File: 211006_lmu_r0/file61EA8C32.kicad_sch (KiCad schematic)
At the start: 15 parts, among them U7 ADuM7641A

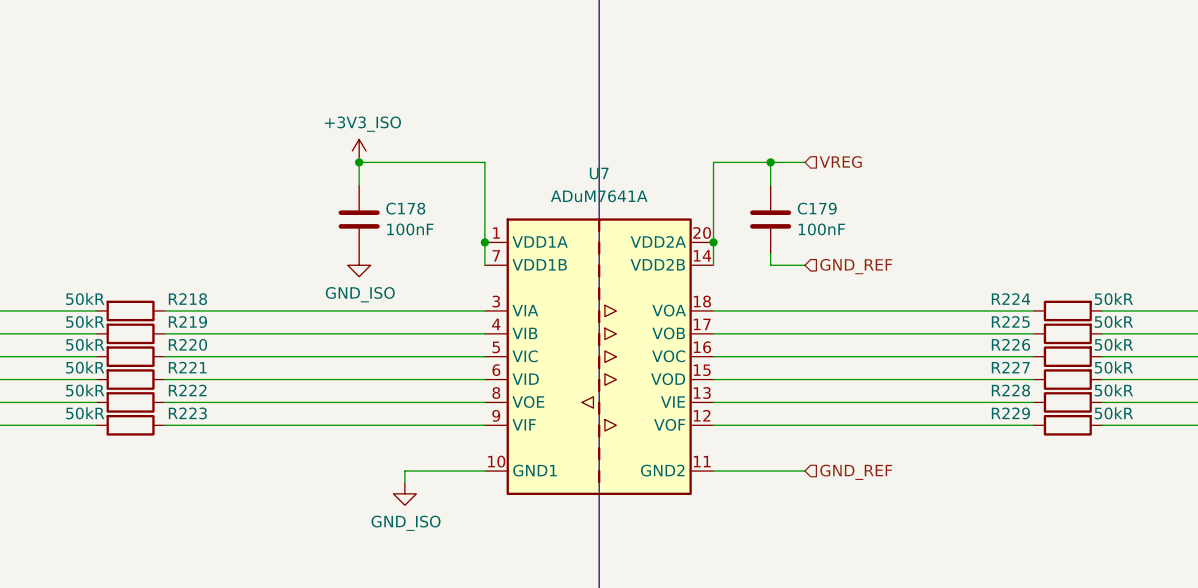
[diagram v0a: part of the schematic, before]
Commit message: moved micro into position
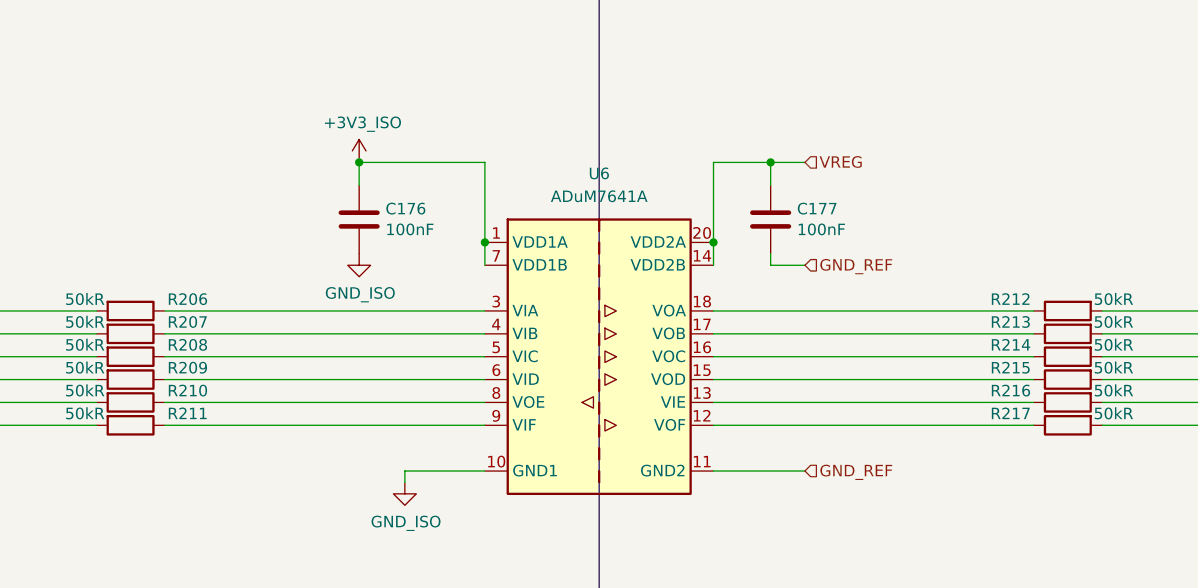
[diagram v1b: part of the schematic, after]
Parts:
- renumbered C178 to C176, C179 to C177, R218 to R206, R219 to R207, R220 to R208, R221 to R209, R222 to R210, R223 to R211, R224 to R212, R225 to R213, R226 to R214, R227 to R215, R228 to R216, R229 to R217, U7 to U6
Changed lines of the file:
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@@
   (symbol (lib_id "Device:C") (at 118.11 83.82 0)
     (in_bom yes) (on_board yes)
-    (property "Reference" "C178" (id 0) (at 121.031 82.6516 0)
+    (property "Reference" "C176" (id 0) (at 121.031 82.6516 0)
       (effects (font (size 1.27 1.27)) (justify left))
     )
@@
   (symbol (lib_id "Device:R") (at 92.71 101.6 270)
     (in_bom yes) (on_board yes)
-    (property "Reference" "R221" (id 0) (at 99.06 100.33 90))
+    (property "Reference" "R209" (id 0) (at 99.06 100.33 90))
     (property "Value" "50kR" (id 1) (at 87.63 100.33 90))
     (property "Footprint" "Resistor_SMD:R_0603_1608Metric_Pad0.98x0.95mm_HandSolder" (id 2) (at 92.71 99.822 90)
@@
   (symbol (lib_id "Device:R") (at 92.71 93.98 270)
     (in_bom yes) (on_board yes)
-    (property "Reference" "R218" (id 0) (at 99.06 92.71 90))
+    (property "Reference" "R206" (id 0) (at 99.06 92.71 90))
     (property "Value" "50kR" (id 1) (at 87.63 92.71 90))
     (property "Footprint" "Resistor_SMD:R_0603_1608Metric_Pad0.98x0.95mm_HandSolder" (id 2) (at 92.71 92.202 90)
@@
   (symbol (lib_id "Device:R") (at 196.85 99.06 90) (mirror x)
     (in_bom yes) (on_board yes)
-    (property "Reference" "R226" (id 0) (at 190.5 97.79 90))
+    (property "Reference" "R214" (id 0) (at 190.5 97.79 90))
     (property "Value" "50kR" (id 1) (at 201.93 97.79 90))
     (property "Footprint" "Resistor_SMD:R_0603_1608Metric_Pad0.98x0.95mm_HandSolder" (id 2) (at 196.85 97.282 90)
@@
   (symbol (lib_id "Device:R") (at 92.71 99.06 270)
     (in_bom yes) (on_board yes)
-    (property "Reference" "R220" (id 0) (at 99.06 97.79 90))
+    (property "Reference" "R208" (id 0) (at 99.06 97.79 90))
     (property "Value" "50kR" (id 1) (at 87.63 97.79 90))
     (property "Footprint" "Resistor_SMD:R_0603_1608Metric_Pad0.98x0.95mm_HandSolder" (id 2) (at 92.71 97.282 90)
@@
   (symbol (lib_id "Device:R") (at 92.71 106.68 270)
     (in_bom yes) (on_board yes)
-    (property "Reference" "R223" (id 0) (at 99.06 105.41 90))
+    (property "Reference" "R211" (id 0) (at 99.06 105.41 90))
     (property "Value" "50kR" (id 1) (at 87.63 105.41 90))
     (property "Footprint" "Resistor_SMD:R_0603_1608Metric_Pad0.98x0.95mm_HandSolder" (id 2) (at 92.71 104.902 90)
@@
   (symbol (lib_id "Device:R") (at 92.71 96.52 270)
     (in_bom yes) (on_board yes)
-    (property "Reference" "R219" (id 0) (at 99.06 95.25 90))
+    (property "Reference" "R207" (id 0) (at 99.06 95.25 90))
     (property "Value" "50kR" (id 1) (at 87.63 95.25 90))
     (property "Footprint" "Resistor_SMD:R_0603_1608Metric_Pad0.98x0.95mm_HandSolder" (id 2) (at 92.71 94.742 90)
@@
   (symbol (lib_id "Device:R") (at 196.85 93.98 90) (mirror x)
     (in_bom yes) (on_board yes)
-    (property "Reference" "R224" (id 0) (at 190.5 92.71 90))
+    (property "Reference" "R212" (id 0) (at 190.5 92.71 90))
     (property "Value" "50kR" (id 1) (at 201.93 92.71 90))
     (property "Footprint" "Resistor_SMD:R_0603_1608Metric_Pad0.98x0.95mm_HandSolder" (id 2) (at 196.85 92.202 90)
@@
   (symbol (lib_id "Isolator:ADuM7641A") (at 144.78 99.06 0)
     (in_bom yes) (on_board yes) (fields_autoplaced)
-    (property "Reference" "U7" (id 0) (at 144.78 78.74 0))
+    (property "Reference" "U6" (id 0) (at 144.78 78.74 0))
     (property "Value" "ADuM7641A" (id 1) (at 144.78 81.28 0))
     (property "Footprint" "Package_SO:QSOP-20_3.9x8.7mm_P0.635mm" (id 2) (at 144.78 116.84 0)
@@
   (symbol (lib_id "Device:R") (at 196.85 101.6 90) (mirror x)
     (in_bom yes) (on_board yes)
-    (property "Reference" "R227" (id 0) (at 190.5 100.33 90))
+    (property "Reference" "R215" (id 0) (at 190.5 100.33 90))
     (property "Value" "50kR" (id 1) (at 201.93 100.33 90))
     (property "Footprint" "Resistor_SMD:R_0603_1608Metric_Pad0.98x0.95mm_HandSolder" (id 2) (at 196.85 99.822 90)
@@
   (symbol (lib_id "Device:R") (at 92.71 104.14 270)
     (in_bom yes) (on_board yes)
-    (property "Reference" "R222" (id 0) (at 99.06 102.87 90))
+    (property "Reference" "R210" (id 0) (at 99.06 102.87 90))
     (property "Value" "50kR" (id 1) (at 87.63 102.87 90))
     (property "Footprint" "Resistor_SMD:R_0603_1608Metric_Pad0.98x0.95mm_HandSolder" (id 2) (at 92.71 102.362 90)
@@
   (symbol (lib_id "Device:R") (at 196.85 96.52 90) (mirror x)
     (in_bom yes) (on_board yes)
-    (property "Reference" "R225" (id 0) (at 190.5 95.25 90))
+    (property "Reference" "R213" (id 0) (at 190.5 95.25 90))
     (property "Value" "50kR" (id 1) (at 201.93 95.25 90))
     (property "Footprint" "Resistor_SMD:R_0603_1608Metric_Pad0.98x0.95mm_HandSolder" (id 2) (at 196.85 94.742 90)
@@
   (symbol (lib_id "Device:R") (at 196.85 104.14 90) (mirror x)
     (in_bom yes) (on_board yes)
-    (property "Reference" "R228" (id 0) (at 190.5 102.87 90))
+    (property "Reference" "R216" (id 0) (at 190.5 102.87 90))
     (property "Value" "50kR" (id 1) (at 201.93 102.87 90))
     (property "Footprint" "Resistor_SMD:R_0603_1608Metric_Pad0.98x0.95mm_HandSolder" (id 2) (at 196.85 102.362 90)
@@
   (symbol (lib_id "Device:C") (at 163.83 83.82 0)
     (in_bom yes) (on_board yes)
-    (property "Reference" "C179" (id 0) (at 166.751 82.6516 0)
+    (property "Reference" "C177" (id 0) (at 166.751 82.6516 0)
       (effects (font (size 1.27 1.27)) (justify left))
     )
@@
   (symbol (lib_id "Device:R") (at 196.85 106.68 90) (mirror x)
     (in_bom yes) (on_board yes)
-    (property "Reference" "R229" (id 0) (at 190.5 105.41 90))
+    (property "Reference" "R217" (id 0) (at 190.5 105.41 90))
     (property "Value" "50kR" (id 1) (at 201.93 105.41 90))
     (property "Footprint" "Resistor_SMD:R_0603_1608Metric_Pad0.98x0.95mm_HandSolder" (id 2) (at 196.85 104.902 90)

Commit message: routed ltc3811 accessories
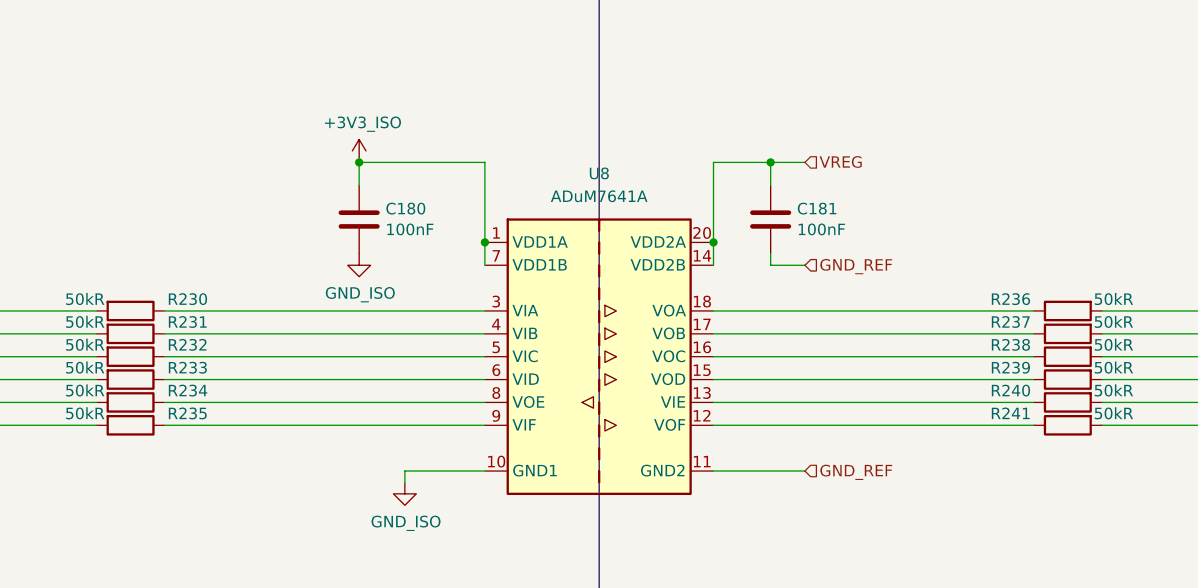
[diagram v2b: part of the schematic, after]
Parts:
- renumbered C176 to C180, C177 to C181, R206 to R230, R207 to R231, R208 to R232, R209 to R233, R210 to R234, R211 to R235, R212 to R236, R213 to R237, R214 to R238, R215 to R239, R216 to R240, R217 to R241, U6 to U8
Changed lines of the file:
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@@
   (symbol (lib_id "Device:C") (at 118.11 83.82 0)
     (in_bom yes) (on_board yes)
-    (property "Reference" "C176" (id 0) (at 121.031 82.6516 0)
+    (property "Reference" "C180" (id 0) (at 121.031 82.6516 0)
       (effects (font (size 1.27 1.27)) (justify left))
     )
@@
   (symbol (lib_id "Device:R") (at 92.71 101.6 270)
     (in_bom yes) (on_board yes)
-    (property "Reference" "R209" (id 0) (at 99.06 100.33 90))
+    (property "Reference" "R233" (id 0) (at 99.06 100.33 90))
     (property "Value" "50kR" (id 1) (at 87.63 100.33 90))
     (property "Footprint" "Resistor_SMD:R_0603_1608Metric_Pad0.98x0.95mm_HandSolder" (id 2) (at 92.71 99.822 90)
@@
   (symbol (lib_id "Device:R") (at 92.71 93.98 270)
     (in_bom yes) (on_board yes)
-    (property "Reference" "R206" (id 0) (at 99.06 92.71 90))
+    (property "Reference" "R230" (id 0) (at 99.06 92.71 90))
     (property "Value" "50kR" (id 1) (at 87.63 92.71 90))
     (property "Footprint" "Resistor_SMD:R_0603_1608Metric_Pad0.98x0.95mm_HandSolder" (id 2) (at 92.71 92.202 90)
@@
   (symbol (lib_id "Device:R") (at 196.85 99.06 90) (mirror x)
     (in_bom yes) (on_board yes)
-    (property "Reference" "R214" (id 0) (at 190.5 97.79 90))
+    (property "Reference" "R238" (id 0) (at 190.5 97.79 90))
     (property "Value" "50kR" (id 1) (at 201.93 97.79 90))
     (property "Footprint" "Resistor_SMD:R_0603_1608Metric_Pad0.98x0.95mm_HandSolder" (id 2) (at 196.85 97.282 90)
@@
   (symbol (lib_id "Device:R") (at 92.71 99.06 270)
     (in_bom yes) (on_board yes)
-    (property "Reference" "R208" (id 0) (at 99.06 97.79 90))
+    (property "Reference" "R232" (id 0) (at 99.06 97.79 90))
     (property "Value" "50kR" (id 1) (at 87.63 97.79 90))
     (property "Footprint" "Resistor_SMD:R_0603_1608Metric_Pad0.98x0.95mm_HandSolder" (id 2) (at 92.71 97.282 90)
@@
   (symbol (lib_id "Device:R") (at 92.71 106.68 270)
     (in_bom yes) (on_board yes)
-    (property "Reference" "R211" (id 0) (at 99.06 105.41 90))
+    (property "Reference" "R235" (id 0) (at 99.06 105.41 90))
     (property "Value" "50kR" (id 1) (at 87.63 105.41 90))
     (property "Footprint" "Resistor_SMD:R_0603_1608Metric_Pad0.98x0.95mm_HandSolder" (id 2) (at 92.71 104.902 90)
@@
   (symbol (lib_id "Device:R") (at 92.71 96.52 270)
     (in_bom yes) (on_board yes)
-    (property "Reference" "R207" (id 0) (at 99.06 95.25 90))
+    (property "Reference" "R231" (id 0) (at 99.06 95.25 90))
     (property "Value" "50kR" (id 1) (at 87.63 95.25 90))
     (property "Footprint" "Resistor_SMD:R_0603_1608Metric_Pad0.98x0.95mm_HandSolder" (id 2) (at 92.71 94.742 90)
@@
   (symbol (lib_id "Device:R") (at 196.85 93.98 90) (mirror x)
     (in_bom yes) (on_board yes)
-    (property "Reference" "R212" (id 0) (at 190.5 92.71 90))
+    (property "Reference" "R236" (id 0) (at 190.5 92.71 90))
     (property "Value" "50kR" (id 1) (at 201.93 92.71 90))
     (property "Footprint" "Resistor_SMD:R_0603_1608Metric_Pad0.98x0.95mm_HandSolder" (id 2) (at 196.85 92.202 90)
@@
   (symbol (lib_id "Isolator:ADuM7641A") (at 144.78 99.06 0)
     (in_bom yes) (on_board yes) (fields_autoplaced)
-    (property "Reference" "U6" (id 0) (at 144.78 78.74 0))
+    (property "Reference" "U8" (id 0) (at 144.78 78.74 0))
     (property "Value" "ADuM7641A" (id 1) (at 144.78 81.28 0))
     (property "Footprint" "Package_SO:QSOP-20_3.9x8.7mm_P0.635mm" (id 2) (at 144.78 116.84 0)
@@
   (symbol (lib_id "Device:R") (at 196.85 101.6 90) (mirror x)
     (in_bom yes) (on_board yes)
-    (property "Reference" "R215" (id 0) (at 190.5 100.33 90))
+    (property "Reference" "R239" (id 0) (at 190.5 100.33 90))
     (property "Value" "50kR" (id 1) (at 201.93 100.33 90))
     (property "Footprint" "Resistor_SMD:R_0603_1608Metric_Pad0.98x0.95mm_HandSolder" (id 2) (at 196.85 99.822 90)
@@
   (symbol (lib_id "Device:R") (at 92.71 104.14 270)
     (in_bom yes) (on_board yes)
-    (property "Reference" "R210" (id 0) (at 99.06 102.87 90))
+    (property "Reference" "R234" (id 0) (at 99.06 102.87 90))
     (property "Value" "50kR" (id 1) (at 87.63 102.87 90))
     (property "Footprint" "Resistor_SMD:R_0603_1608Metric_Pad0.98x0.95mm_HandSolder" (id 2) (at 92.71 102.362 90)
@@
   (symbol (lib_id "Device:R") (at 196.85 96.52 90) (mirror x)
     (in_bom yes) (on_board yes)
-    (property "Reference" "R213" (id 0) (at 190.5 95.25 90))
+    (property "Reference" "R237" (id 0) (at 190.5 95.25 90))
     (property "Value" "50kR" (id 1) (at 201.93 95.25 90))
     (property "Footprint" "Resistor_SMD:R_0603_1608Metric_Pad0.98x0.95mm_HandSolder" (id 2) (at 196.85 94.742 90)
@@
   (symbol (lib_id "Device:R") (at 196.85 104.14 90) (mirror x)
     (in_bom yes) (on_board yes)
-    (property "Reference" "R216" (id 0) (at 190.5 102.87 90))
+    (property "Reference" "R240" (id 0) (at 190.5 102.87 90))
     (property "Value" "50kR" (id 1) (at 201.93 102.87 90))
     (property "Footprint" "Resistor_SMD:R_0603_1608Metric_Pad0.98x0.95mm_HandSolder" (id 2) (at 196.85 102.362 90)
@@
   (symbol (lib_id "Device:C") (at 163.83 83.82 0)
     (in_bom yes) (on_board yes)
-    (property "Reference" "C177" (id 0) (at 166.751 82.6516 0)
+    (property "Reference" "C181" (id 0) (at 166.751 82.6516 0)
       (effects (font (size 1.27 1.27)) (justify left))
     )
@@
   (symbol (lib_id "Device:R") (at 196.85 106.68 90) (mirror x)
     (in_bom yes) (on_board yes)
-    (property "Reference" "R217" (id 0) (at 190.5 105.41 90))
+    (property "Reference" "R241" (id 0) (at 190.5 105.41 90))
     (property "Value" "50kR" (id 1) (at 201.93 105.41 90))
     (property "Footprint" "Resistor_SMD:R_0603_1608Metric_Pad0.98x0.95mm_HandSolder" (id 2) (at 196.85 104.902 90)

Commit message: trying out a quick thing, recover
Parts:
- renumbered C180 to C178, C181 to C179, R230 to R218, R231 to R219, R232 to R220, R233 to R221, R234 to R222, R235 to R223, R236 to R224, R237 to R225, R238 to R226, R239 to R227, R240 to R228, R241 to R229, U8 to U7
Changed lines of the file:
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@@
   (symbol (lib_id "+3v3_iso:+3V3_ISO") (at 118.11 77.47 0)
     (in_bom yes) (on_board yes)
-    (property "Reference" "#PWR0104" (id 0) (at 118.11 81.28 0)
+    (property "Reference" "#PWR0102" (id 0) (at 118.11 81.28 0)
       (effects (font (size 1.27 1.27)) hide)
     )
@@
   (symbol (lib_id "Device:C") (at 118.11 83.82 0)
     (in_bom yes) (on_board yes)
-    (property "Reference" "C180" (id 0) (at 121.031 82.6516 0)
+    (property "Reference" "C178" (id 0) (at 121.031 82.6516 0)
       (effects (font (size 1.27 1.27)) (justify left))
     )
@@
   (symbol (lib_id "Device:R") (at 92.71 101.6 270)
     (in_bom yes) (on_board yes)
-    (property "Reference" "R233" (id 0) (at 99.06 100.33 90))
+    (property "Reference" "R221" (id 0) (at 99.06 100.33 90))
     (property "Value" "50kR" (id 1) (at 87.63 100.33 90))
     (property "Footprint" "Resistor_SMD:R_0603_1608Metric_Pad0.98x0.95mm_HandSolder" (id 2) (at 92.71 99.822 90)
@@
   (symbol (lib_id "Device:R") (at 92.71 93.98 270)
     (in_bom yes) (on_board yes)
-    (property "Reference" "R230" (id 0) (at 99.06 92.71 90))
+    (property "Reference" "R218" (id 0) (at 99.06 92.71 90))
     (property "Value" "50kR" (id 1) (at 87.63 92.71 90))
     (property "Footprint" "Resistor_SMD:R_0603_1608Metric_Pad0.98x0.95mm_HandSolder" (id 2) (at 92.71 92.202 90)
@@
   (symbol (lib_id "Device:R") (at 196.85 99.06 90) (mirror x)
     (in_bom yes) (on_board yes)
-    (property "Reference" "R238" (id 0) (at 190.5 97.79 90))
+    (property "Reference" "R226" (id 0) (at 190.5 97.79 90))
     (property "Value" "50kR" (id 1) (at 201.93 97.79 90))
     (property "Footprint" "Resistor_SMD:R_0603_1608Metric_Pad0.98x0.95mm_HandSolder" (id 2) (at 196.85 97.282 90)
@@
   (symbol (lib_id "Device:R") (at 92.71 99.06 270)
     (in_bom yes) (on_board yes)
-    (property "Reference" "R232" (id 0) (at 99.06 97.79 90))
+    (property "Reference" "R220" (id 0) (at 99.06 97.79 90))
     (property "Value" "50kR" (id 1) (at 87.63 97.79 90))
     (property "Footprint" "Resistor_SMD:R_0603_1608Metric_Pad0.98x0.95mm_HandSolder" (id 2) (at 92.71 97.282 90)
@@
   (symbol (lib_id "Device:R") (at 92.71 106.68 270)
     (in_bom yes) (on_board yes)
-    (property "Reference" "R235" (id 0) (at 99.06 105.41 90))
+    (property "Reference" "R223" (id 0) (at 99.06 105.41 90))
     (property "Value" "50kR" (id 1) (at 87.63 105.41 90))
     (property "Footprint" "Resistor_SMD:R_0603_1608Metric_Pad0.98x0.95mm_HandSolder" (id 2) (at 92.71 104.902 90)
@@
   (symbol (lib_id "Device:R") (at 92.71 96.52 270)
     (in_bom yes) (on_board yes)
-    (property "Reference" "R231" (id 0) (at 99.06 95.25 90))
+    (property "Reference" "R219" (id 0) (at 99.06 95.25 90))
     (property "Value" "50kR" (id 1) (at 87.63 95.25 90))
     (property "Footprint" "Resistor_SMD:R_0603_1608Metric_Pad0.98x0.95mm_HandSolder" (id 2) (at 92.71 94.742 90)
@@
   (symbol (lib_id "Device:R") (at 196.85 93.98 90) (mirror x)
     (in_bom yes) (on_board yes)
-    (property "Reference" "R236" (id 0) (at 190.5 92.71 90))
+    (property "Reference" "R224" (id 0) (at 190.5 92.71 90))
     (property "Value" "50kR" (id 1) (at 201.93 92.71 90))
     (property "Footprint" "Resistor_SMD:R_0603_1608Metric_Pad0.98x0.95mm_HandSolder" (id 2) (at 196.85 92.202 90)
@@
   (symbol (lib_id "Isolator:ADuM7641A") (at 144.78 99.06 0)
     (in_bom yes) (on_board yes) (fields_autoplaced)
-    (property "Reference" "U8" (id 0) (at 144.78 78.74 0))
+    (property "Reference" "U7" (id 0) (at 144.78 78.74 0))
     (property "Value" "ADuM7641A" (id 1) (at 144.78 81.28 0))
     (property "Footprint" "Package_SO:QSOP-20_3.9x8.7mm_P0.635mm" (id 2) (at 144.78 116.84 0)
@@
   (symbol (lib_id "Device:R") (at 196.85 101.6 90) (mirror x)
     (in_bom yes) (on_board yes)
-    (property "Reference" "R239" (id 0) (at 190.5 100.33 90))
+    (property "Reference" "R227" (id 0) (at 190.5 100.33 90))
     (property "Value" "50kR" (id 1) (at 201.93 100.33 90))
     (property "Footprint" "Resistor_SMD:R_0603_1608Metric_Pad0.98x0.95mm_HandSolder" (id 2) (at 196.85 99.822 90)
@@
   (symbol (lib_id "gnd_iso:GND_ISO") (at 123.19 113.03 0)
     (in_bom yes) (on_board yes)
-    (property "Reference" "#PWR019" (id 0) (at 123.19 119.38 0)
+    (property "Reference" "#PWR017" (id 0) (at 123.19 119.38 0)
       (effects (font (size 1.27 1.27)) hide)
     )
@@
   (symbol (lib_id "Device:R") (at 92.71 104.14 270)
     (in_bom yes) (on_board yes)
-    (property "Reference" "R234" (id 0) (at 99.06 102.87 90))
+    (property "Reference" "R222" (id 0) (at 99.06 102.87 90))
     (property "Value" "50kR" (id 1) (at 87.63 102.87 90))
     (property "Footprint" "Resistor_SMD:R_0603_1608Metric_Pad0.98x0.95mm_HandSolder" (id 2) (at 92.71 102.362 90)
@@
   (symbol (lib_id "Device:R") (at 196.85 96.52 90) (mirror x)
     (in_bom yes) (on_board yes)
-    (property "Reference" "R237" (id 0) (at 190.5 95.25 90))
+    (property "Reference" "R225" (id 0) (at 190.5 95.25 90))
     (property "Value" "50kR" (id 1) (at 201.93 95.25 90))
     (property "Footprint" "Resistor_SMD:R_0603_1608Metric_Pad0.98x0.95mm_HandSolder" (id 2) (at 196.85 94.742 90)
@@
   (symbol (lib_id "gnd_iso:GND_ISO") (at 118.11 87.63 0)
     (in_bom yes) (on_board yes)
-    (property "Reference" "#PWR018" (id 0) (at 118.11 93.98 0)
+    (property "Reference" "#PWR016" (id 0) (at 118.11 93.98 0)
       (effects (font (size 1.27 1.27)) hide)
     )
@@
   (symbol (lib_id "Device:R") (at 196.85 104.14 90) (mirror x)
     (in_bom yes) (on_board yes)
-    (property "Reference" "R240" (id 0) (at 190.5 102.87 90))
+    (property "Reference" "R228" (id 0) (at 190.5 102.87 90))
     (property "Value" "50kR" (id 1) (at 201.93 102.87 90))
     (property "Footprint" "Resistor_SMD:R_0603_1608Metric_Pad0.98x0.95mm_HandSolder" (id 2) (at 196.85 102.362 90)
@@
   (symbol (lib_id "Device:C") (at 163.83 83.82 0)
     (in_bom yes) (on_board yes)
-    (property "Reference" "C181" (id 0) (at 166.751 82.6516 0)
+    (property "Reference" "C179" (id 0) (at 166.751 82.6516 0)
       (effects (font (size 1.27 1.27)) (justify left))
     )
@@
   (symbol (lib_id "Device:R") (at 196.85 106.68 90) (mirror x)
     (in_bom yes) (on_board yes)
-    (property "Reference" "R241" (id 0) (at 190.5 105.41 90))
+    (property "Reference" "R229" (id 0) (at 190.5 105.41 90))
     (property "Value" "50kR" (id 1) (at 201.93 105.41 90))
     (property "Footprint" "Resistor_SMD:R_0603_1608Metric_Pad0.98x0.95mm_HandSolder" (id 2) (at 196.85 104.902 90)
